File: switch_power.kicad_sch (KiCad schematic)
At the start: 35 parts, among them X1 25000000

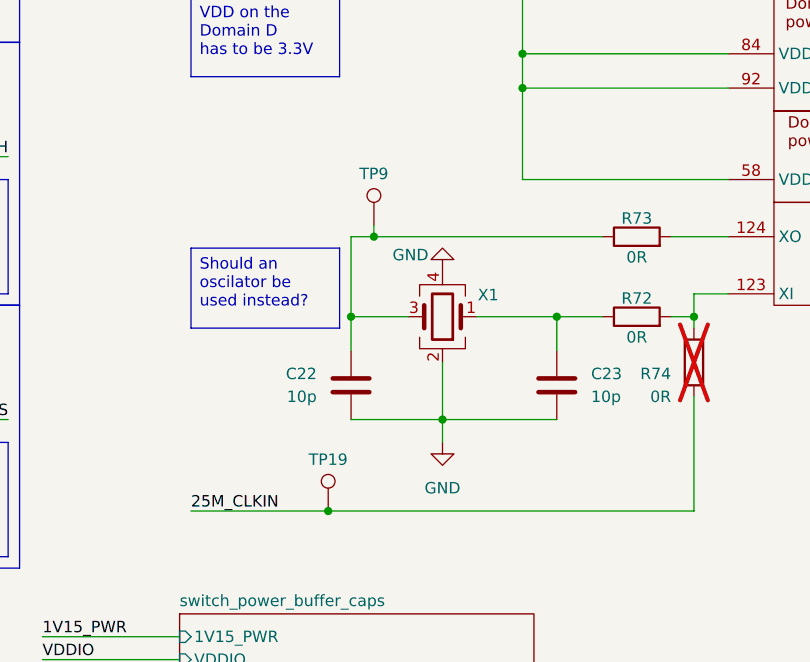
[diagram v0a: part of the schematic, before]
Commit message: Uses crystal sheet in all places. Refs: #1
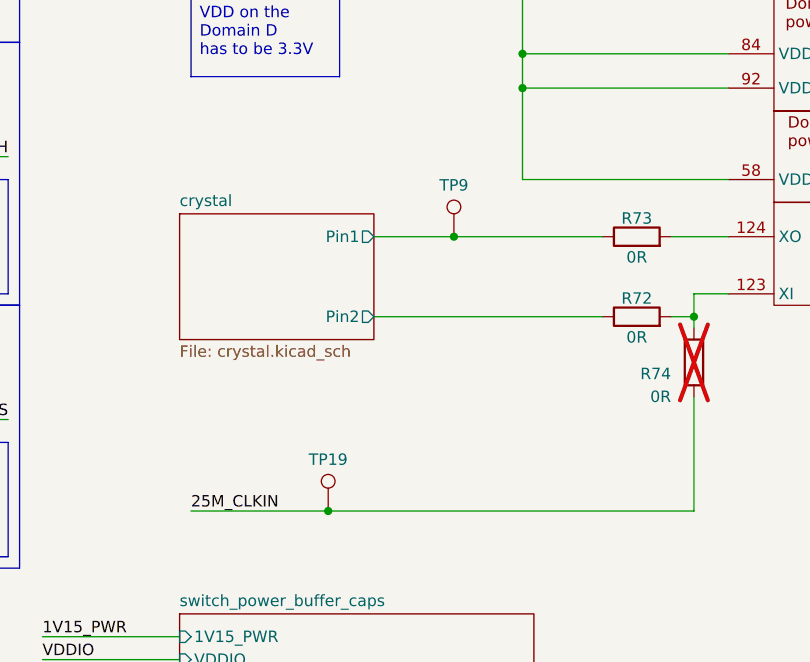
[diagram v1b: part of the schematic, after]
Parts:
- removed C22, C23: 10p, Capacitor_SMD:C_0201_0603Metric, symbol KL_C:C_10p_25V_C0G_0603_5
- removed X1: 25000000, symbol KL_Passive_ICs:Crystal_25MHz_32p
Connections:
- net crystal/Pin2: now reaches R72.1
- net crystal/Pin1: now reaches R73.1, TP9.1
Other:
- added sheet crystal (crystal.kicad_sch)
- moved on the sheet: TP9

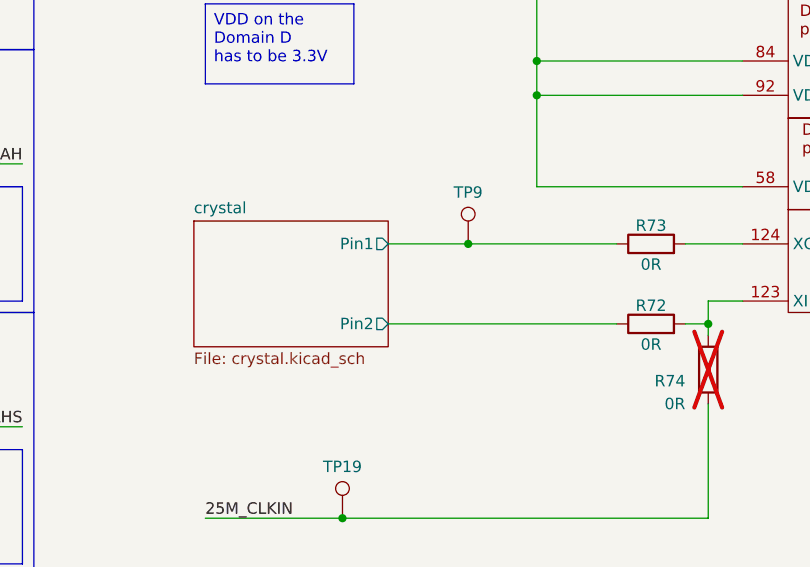
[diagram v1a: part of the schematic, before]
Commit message: modularizes xtal at STM and switch power. Refs: #1
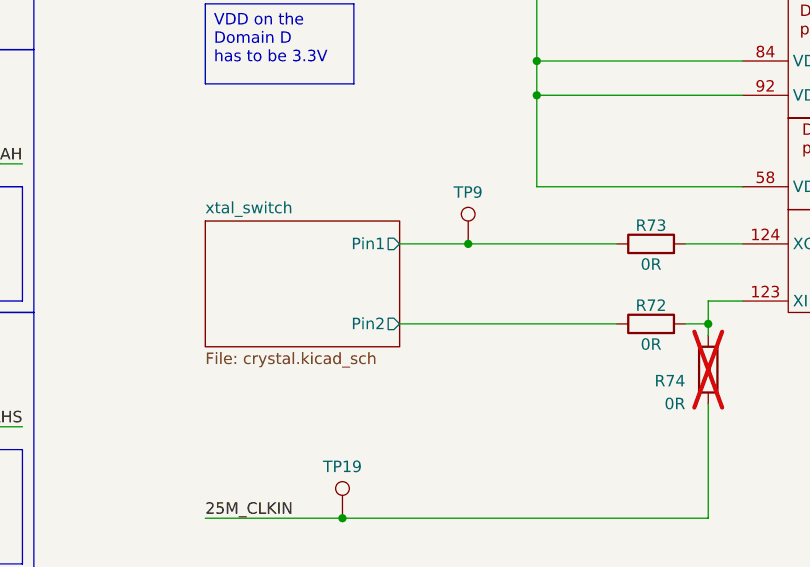
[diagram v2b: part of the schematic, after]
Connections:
- net crystal/Pin1 renamed xtal_switch/Pin1
- net crystal/Pin2 renamed xtal_switch/Pin2
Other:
- removed sheet crystal
- added sheet xtal_switch (crystal.kicad_sch)
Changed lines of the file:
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@@
 	(wire
 		(pts
-			(xy 125.73 138.43) (xy 151.13 138.43)
-		)
-		(stroke
-			(width 0)
-			(type default)
-		)
-	)
-	(wire
-		(pts
 			(xy 205.74 107.95) (xy 232.41 107.95)
 		)
@@
 	(wire
 		(pts
+			(xy 127 138.43) (xy 151.13 138.43)
+		)
+		(stroke
+			(width 0)
+			(type default)
+		)
+	)
+	(wire
+		(pts
 			(xy 50.8 62.23) (xy 53.34 62.23)
 		)
@@
 	(wire
 		(pts
+			(xy 127 129.54) (xy 134.62 129.54)
+		)
+		(stroke
+			(width 0)
+			(type default)
+		)
+	)
+	(wire
+		(pts
 			(xy 50.8 91.44) (xy 53.34 91.44)
 		)
@@
 	(wire
 		(pts
-			(xy 125.73 129.54) (xy 134.62 129.54)
-		)
-		(stroke
-			(width 0)
-			(type default)
-		)
-	)
-	(wire
-		(pts
 			(xy 149.86 55.88) (xy 165.1 55.88)
 		)
@@
 	)
 	(sheet
-		(at 104.14 127)
+		(at 105.41 127)
 		(size 21.59 13.97)
 		(exclude_from_sim no)
@@
 			(color 0 0 0 0.0000)
 		)
-		(property "Sheetname" "crystal"
-			(at 104.14 126.2884 0)
+		(property "Sheetname" "xtal_switch"
+			(at 105.41 126.2884 0)
 			(effects
 				(font
@@
 		)
 		(property "Sheetfile" "crystal.kicad_sch"
-			(at 104.14 141.5546 0)
+			(at 105.41 141.5546 0)
 			(effects
 				(font
@@
 		)
 		(pin "Pin1" output
-			(at 125.73 129.54 0)
+			(at 127 129.54 0)
 			(effects
 				(font
@@
 		)
 		(pin "Pin2" output
-			(at 125.73 138.43 0)
+			(at 127 138.43 0)
 			(effects
 				(font
@@
 			(project "shish-lan"
 				(path "/d4536448-b109-4159-96e2-3dc21baf2d6e/0b7d9af9-83c1-43fa-a7a0-a33d0a00ea9c/d7edf10b-e7e7-437a-ab6c-966f29ad8f7f"
-					(page "18")
+					(page "15")
 				)
 			)

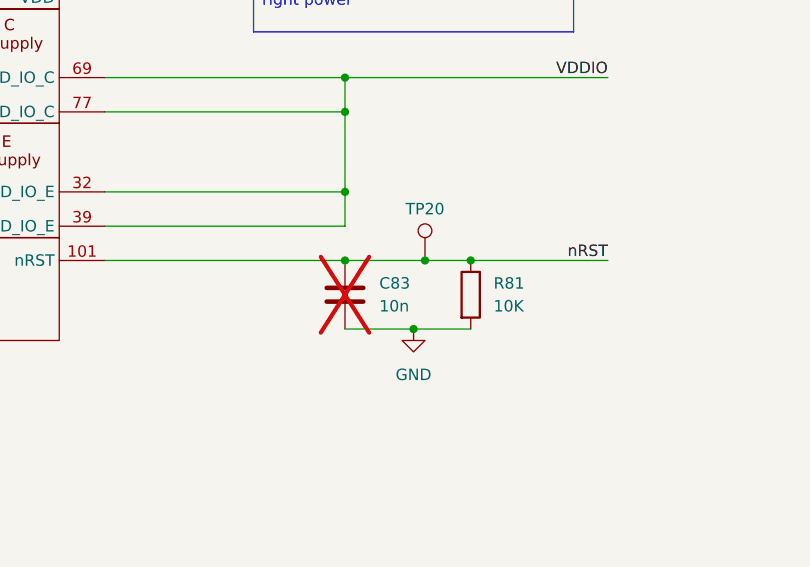
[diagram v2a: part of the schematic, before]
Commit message: fixes duplicate c83. Refs: #1
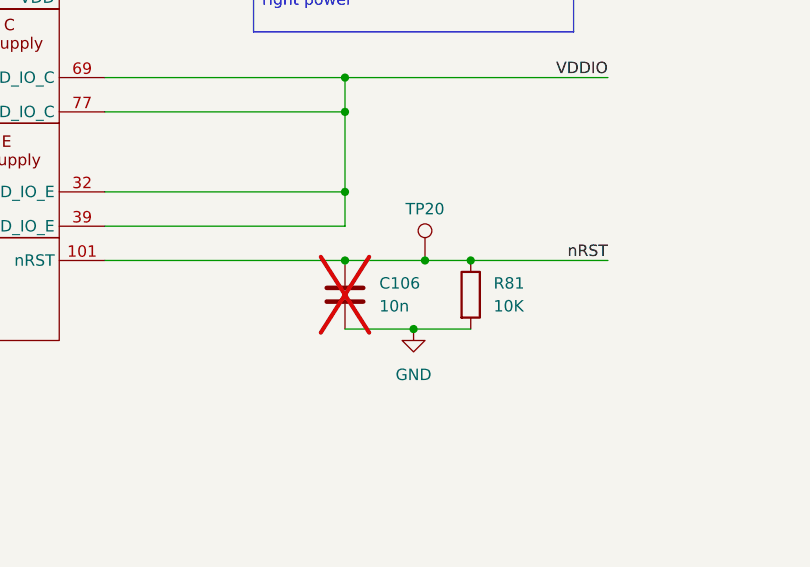
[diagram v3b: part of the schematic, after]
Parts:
- removed C83: 10n, Capacitor_SMD:C_0201_0603Metric, symbol KL_C:C_10n_50V_X7R_0603_10
- added C106: 10n, Capacitor_SMD:C_0201_0603Metric, symbol KL_C:C_10n_50V_X7R_0603_10
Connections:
- net GND: now also C106.2
- net nRST: now also C106.1
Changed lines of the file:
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@@
 	)
 	(junction
-		(at 232.41 128.27)
-		(diameter 0)
-		(color 0 0 0 0)
-	)
-	(junction
 		(at 240.03 135.89)
 		(diameter 0)
@@
 	)
 	(junction
+		(at 232.41 128.27)
+		(diameter 0)
+		(color 0 0 0 0)
+	)
+	(junction
 		(at 142.24 99.06)
 		(diameter 0)
@@
 	(wire
 		(pts
+			(xy 232.41 128.27) (xy 241.3 128.27)
+		)
+		(stroke
+			(width 0)
+			(type default)
+		)
+	)
+	(wire
+		(pts
 			(xy 205.74 41.91) (xy 222.25 41.91)
 		)
@@
 	(wire
 		(pts
-			(xy 232.41 128.27) (xy 241.3 128.27)
+			(xy 205.74 128.27) (xy 232.41 128.27)
 		)
 		(stroke
@@
 	(wire
 		(pts
-			(xy 205.74 128.27) (xy 232.41 128.27)
-		)
-		(stroke
-			(width 0)
-			(type default)
-		)
-	)
-	(wire
-		(pts
 			(xy 88.9 186.69) (xy 104.14 186.69)
 		)
@@
 		(dnp yes)
 		(fields_autoplaced yes)
-		(property "Reference" "C83"
+		(property "Reference" "C106"
 			(at 236.22 130.8099 0)
 			(effects
@@
 		)
 		(instances
-			(project "switch"
-				(path "/cd936d40-9035-4ec8-bcf8-38758f995fb0/d7edf10b-e7e7-437a-ab6c-966f29ad8f7f"
-					(reference "C?")
-					(unit 1)
-				)
-			)
 			(project "shish-lan"
 				(path "/d4536448-b109-4159-96e2-3dc21baf2d6e/0b7d9af9-83c1-43fa-a7a0-a33d0a00ea9c/d7edf10b-e7e7-437a-ab6c-966f29ad8f7f"
-					(reference "C83")
+					(reference "C106")
 					(unit 1)
 				)
@@
 		(on_board yes)
 		(dnp no)
+		(fields_autoplaced yes)
 		(property "Reference" "C20"
 			(at 47.498 68.58 0)

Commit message: fixes ERC errors in DC/DC converters
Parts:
- R81: footprint KL_Footprints:C_0603 -> KL_Footprints:R_0603
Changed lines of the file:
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@@
 			)
 		)
-		(property "Footprint" "KL_Footprints:C_0603"
+		(property "Footprint" "KL_Footprints:R_0603"
 			(at 244.602 132.08 90)
 			(effects

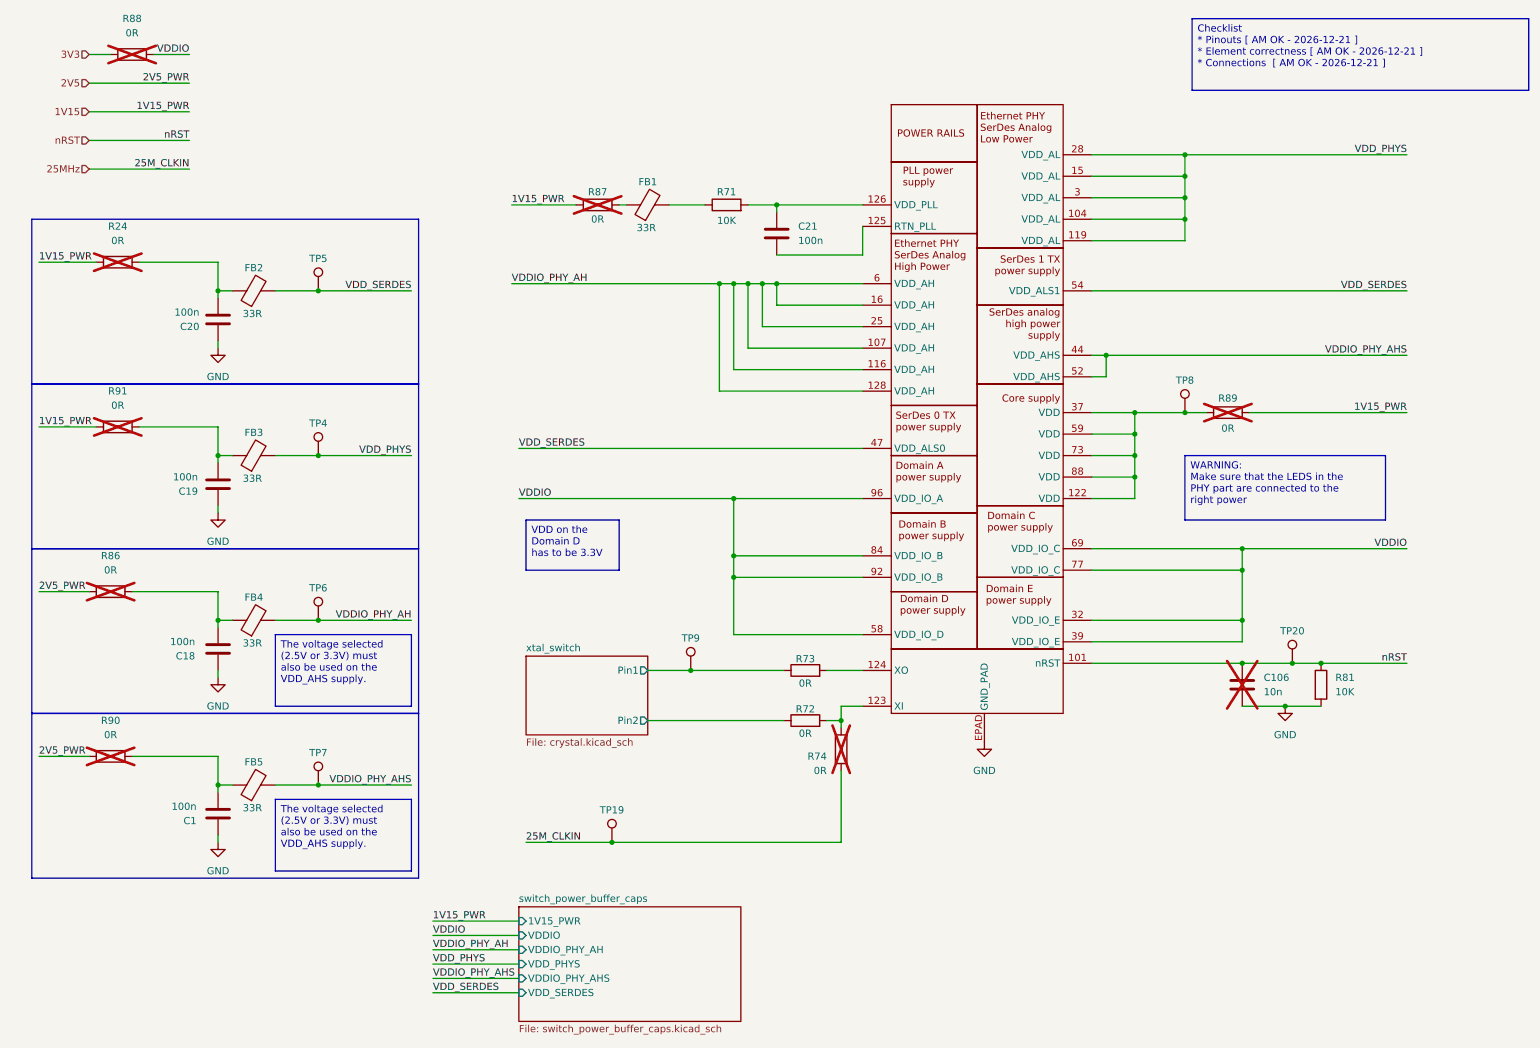
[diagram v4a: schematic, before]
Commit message: updates components from my library misconfiguration. Refs: #1
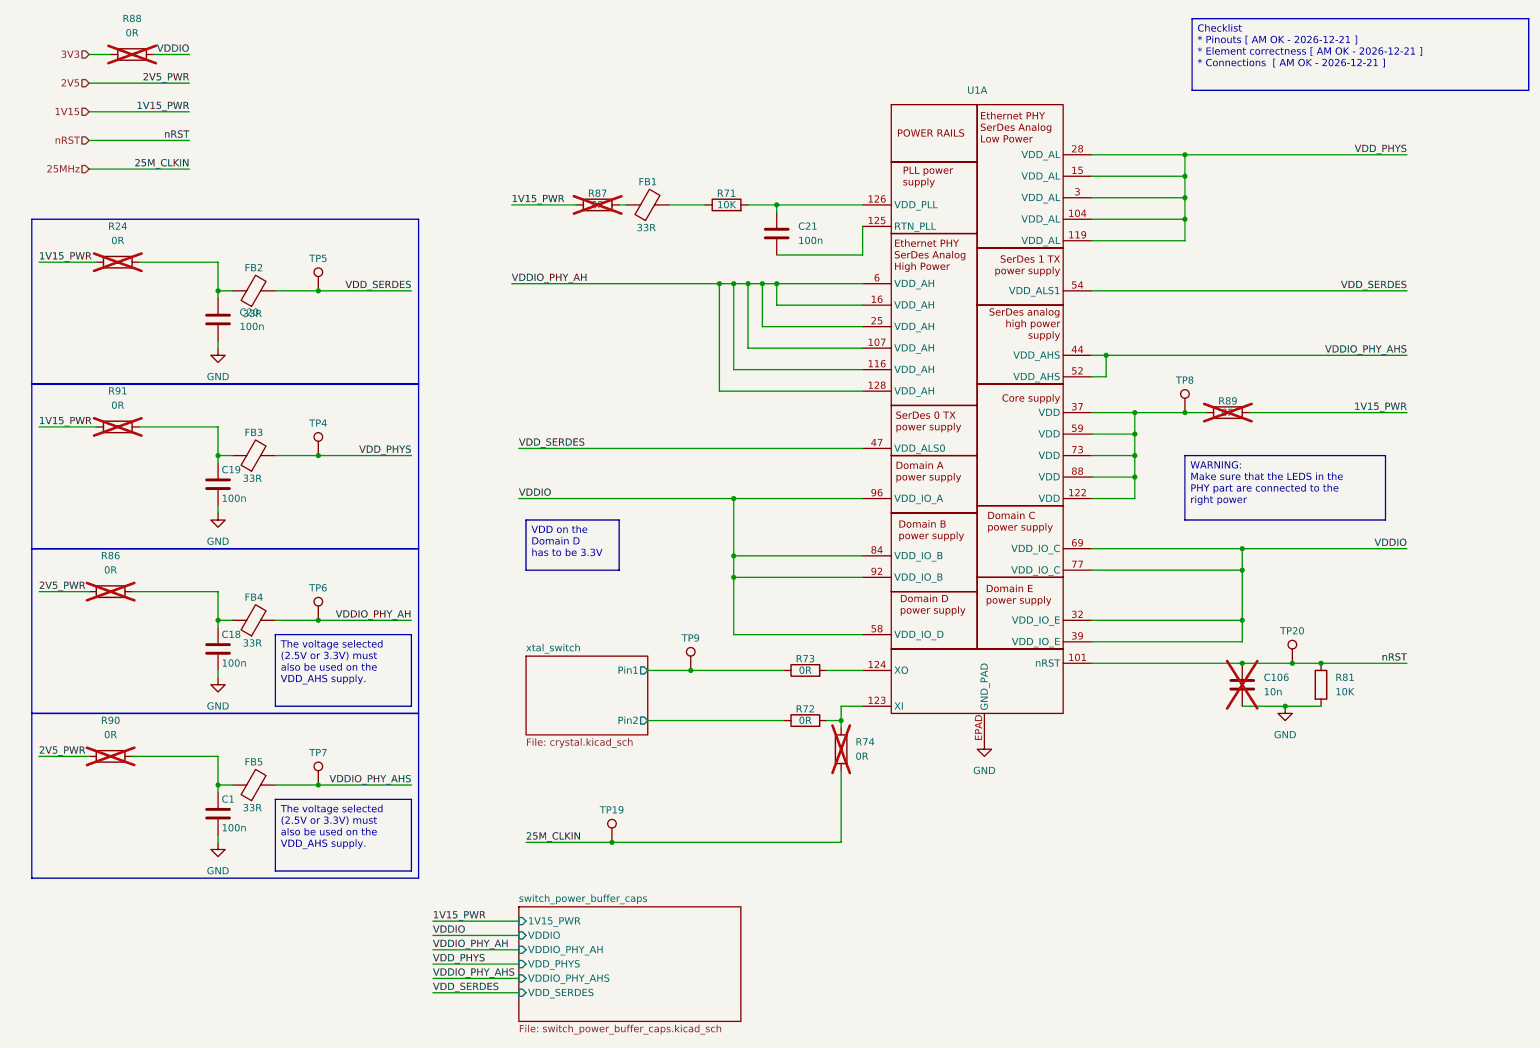
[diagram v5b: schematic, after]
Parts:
- C1, C18, C19, C20, C21: footprint Capacitor_SMD:C_0201_0603Metric -> KL_Footprints:C_0603
- C106: footprint Capacitor_SMD:C_0201_0603Metric -> KL_Footprints:C_0603; now in the parts list
- R71, R72, R73: footprint KL_Footprints:C_0603 -> KL_Footprints:R_0603
- R74: footprint KL_Footprints:C_0603 -> KL_Footprints:R_0603; now in the parts list
- U1: footprint Package_QFP:TQFP-128_14x14mm_P0.4mm -> KL_Footprints:TQFP-128_14x14mm_P0.4mm
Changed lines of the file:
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@@
 		(dnp no)
 		(property "Reference" "R71"
-			(at 140.97 44.704 90)
+			(at 140.97 44.958 90)
 			(effects
 				(font
@@
 		)
 		(property "Value" "10K"
-			(at 140.97 49.784 90)
+			(at 140.97 46.99 90)
 			(effects
 				(font
@@
 			)
 		)
-		(property "Footprint" "KL_Footprints:C_0603"
+		(property "Footprint" "KL_Footprints:R_0603"
 			(at 140.97 48.768 90)
 			(effects
@@
 		(fields_autoplaced yes)
 		(property "Reference" "U1"
-			(at 185.42 27.94 0)
+			(at 185.42 26.67 0)
 			(effects
 				(font
 					(size 1.27 1.27)
 				)
-				(hide yes)
 			)
 		)
@@
 					(size 1.27 1.27)
 				)
+				(hide yes)
 			)
 		)
-		(property "Footprint" "Package_QFP:TQFP-128_14x14mm_P0.4mm"
+		(property "Footprint" "KL_Footprints:TQFP-128_14x14mm_P0.4mm"
 			(at 186.182 25.908 0)
 			(effects
@@
 		)
 		(property "Value" "0R"
-			(at 154.94 131.826 90)
+			(at 154.94 129.54 90)
 			(effects
 				(font
@@
 			)
 		)
-		(property "Footprint" "KL_Footprints:C_0603"
+		(property "Footprint" "KL_Footprints:R_0603"
 			(at 154.94 131.318 90)
 			(effects
@@
 		(unit 1)
 		(exclude_from_sim no)
-		(in_bom no)
+		(in_bom yes)
 		(on_board yes)
 		(dnp yes)
@@
 			)
 		)
-		(property "Footprint" "Capacitor_SMD:C_0201_0603Metric"
+		(property "Footprint" "KL_Footprints:C_0603"
 			(at 233.3752 135.89 0)
 			(effects
@@
 		(dnp yes)
 		(property "Reference" "R89"
-			(at 229.87 81.28 90)
+			(at 229.87 81.788 90)
 			(effects
 				(font
@@
 		)
 		(property "Value" "0R"
-			(at 229.87 86.614 90)
+			(at 229.87 83.82 90)
 			(effects
 				(font
@@
 		)
 		(property "Value" "0R"
-			(at 154.94 140.716 90)
+			(at 154.94 138.43 90)
 			(effects
 				(font
@@
 			)
 		)
-		(property "Footprint" "KL_Footprints:C_0603"
+		(property "Footprint" "KL_Footprints:R_0603"
 			(at 154.94 140.208 90)
 			(effects
@@
 		(dnp no)
 		(property "Reference" "C18"
-			(at 46.736 127 0)
+			(at 51.435 123.19 0)
 			(effects
 				(font
 					(size 1.27 1.27)
 				)
-				(justify right)
+				(justify left)
 			)
 		)
 		(property "Value" "100n"
-			(at 46.736 124.46 0)
+			(at 51.435 128.27 0)
 			(effects
 				(font
 					(size 1.27 1.27)
 				)
-				(justify right)
+				(justify left)
 			)
 		)
-		(property "Footprint" "Capacitor_SMD:C_0201_0603Metric"
+		(property "Footprint" "KL_Footprints:C_0603"
 			(at 51.7652 129.54 0)
 			(effects
@@
 		(dnp no)
 		(property "Reference" "C19"
-			(at 47.244 97.79 0)
+			(at 51.435 93.98 0)
 			(effects
 				(font
 					(size 1.27 1.27)
 				)
-				(justify right)
+				(justify left)
 			)
 		)
 		(property "Value" "100n"
-			(at 47.244 95.25 0)
+			(at 51.435 99.06 0)
 			(effects
 				(font
 					(size 1.27 1.27)
 				)
-				(justify right)
+				(justify left)
 			)
 		)
-		(property "Footprint" "Capacitor_SMD:C_0201_0603Metric"
+		(property "Footprint" "KL_Footprints:C_0603"
 			(at 51.7652 100.33 0)
 			(effects
@@
 		(dnp yes)
 		(property "Reference" "R87"
-			(at 118.11 44.704 90)
+			(at 118.11 44.958 90)
 			(effects
 				(font
@@
 		)
 		(property "Value" "0R"
-			(at 118.11 49.53 90)
+			(at 118.11 46.99 90)
 			(effects
 				(font
@@
 		(dnp no)
 		(property "Reference" "C1"
-			(at 46.99 156.21 0)
+			(at 51.435 152.4 0)
 			(effects
 				(font
 					(size 1.27 1.27)
 				)
-				(justify right)
+				(justify left)
 			)
 		)
 		(property "Value" "100n"
-			(at 46.99 153.67 0)
+			(at 51.435 157.48 0)
 			(effects
 				(font
 					(size 1.27 1.27)
 				)
-				(justify right)
+				(justify left)
 			)
 		)
-		(property "Footprint" "Capacitor_SMD:C_0201_0603Metric"
+		(property "Footprint" "KL_Footprints:C_0603"
 			(at 51.7652 158.75 0)
 			(effects
@@
 		(fields_autoplaced yes)
 		(property "Reference" "C20"
-			(at 47.498 68.58 0)
+			(at 54.61 66.0399 0)
 			(effects
 				(font
 					(size 1.27 1.27)
 				)
-				(justify right)
+				(justify left)
 			)
 		)
 		(property "Value" "100n"
-			(at 47.498 66.04 0)
+			(at 54.61 68.5799 0)
 			(effects
 				(font
 					(size 1.27 1.27)
 				)
-				(justify right)
+				(justify left)
 			)
 		)
-		(property "Footprint" "Capacitor_SMD:C_0201_0603Metric"
+		(property "Footprint" "KL_Footprints:C_0603"
 			(at 51.7652 71.12 0)
 			(effects
@@
 		(unit 1)
 		(exclude_from_sim no)
-		(in_bom no)
+		(in_bom yes)
 		(on_board yes)
 		(dnp yes)
 		(fields_autoplaced yes)
 		(property "Reference" "R74"
-			(at 158.75 144.7799 0)
+			(at 163.83 142.2399 0)
 			(effects
 				(font
 					(size 1.27 1.27)
 				)
-				(justify left)
+				(justify right)
 			)
 		)
 		(property "Value" "0R"
-			(at 158.75 147.3199 0)
+			(at 163.83 144.7799 0)
 			(effects
 				(font
 					(size 1.27 1.27)
 				)
-				(justify left)
+				(justify right)
 			)
 		)
-		(property "Footprint" "KL_Footprints:C_0603"
+		(property "Footprint" "KL_Footprints:R_0603"
 			(at 163.068 143.51 90)
 			(effects
@@
 			)
 		)
-		(property "Footprint" "Capacitor_SMD:C_0201_0603Metric"
+		(property "Footprint" "KL_Footprints:C_0603"
 			(at 150.8252 55.88 0)
 			(effects
